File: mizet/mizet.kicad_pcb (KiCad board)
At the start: 2 copper layers, 41 parts, among them J1 USB_C_Receptacle_USB2.0_16P, J2 Conn_01x04, J3 Conn_01x12, J4 Conn_01x12, SW1 RotaryEncoder_Switch_MP, SW2 SW_Push, SW3 SW_Push, SW4 SW_Push, SW5 SW_Push, U1 RP2040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

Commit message: basic pcb
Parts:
- removed the R5 at (57.8, 52.1)
- removed the U2 at (55.0, 34.7)
- added D1: D_Schottky, Diode_SMD:D_SOD-123, B.Cu at (134.2, 87.8)
- added U1: XC6206PxxxMR, Package_TO_SOT_SMD:SOT-23-3, B.Cu at (135.9, 84.3)
- C1, C17, C2, J1, TP3, TP4, Y1: moved to B.Cu
- C10: renamed from C7; moved to B.Cu
- C11: renamed from C8; moved to B.Cu
- C12: renamed from C9; moved to B.Cu
- C13: renamed from C10; moved to B.Cu
- C14: renamed from C11; moved to B.Cu
- C15: renamed from C12; moved to B.Cu
- C16: renamed from C13; moved to B.Cu
- C3: renamed from C14; moved to B.Cu
- C4: renamed from C15; moved to B.Cu
- C5: renamed from C16; moved to B.Cu
- C6: renamed from C3; moved to B.Cu
- C7: renamed from C4; moved to B.Cu
- C8: renamed from C5; moved to B.Cu
- C9: renamed from C6; moved to B.Cu
- J3, J4: footprint Connector_PinSocket_2.54mm:PinSocket_1x12_P2.54mm_Vertical -> Connector_PinHeader_2.54mm:PinHeader_1x12_P2.54mm_Vertical; moved to B.Cu
- R1: renamed from R3; moved to B.Cu
- R2: renamed from R4; moved to B.Cu
- R3: renamed from R1; moved to B.Cu
- R4: renamed from R2; moved to B.Cu
- R5: renamed from R6; moved to B.Cu
- R6: renamed from R7; moved to B.Cu
- SW2, SW3, SW4, SW5: footprint Button_Switch_THT:SW_PUSH_1P1T_6x3.5mm_H4.3_APEM_MJTP1243 -> My_lib:tact_sw_smd
- TP1: renamed from TP2; moved to B.Cu
- TP2: renamed from TP1; moved to B.Cu
- U2: renamed from U1; footprint Package_DFN_QFN:QFN-56-1EP_7x7mm_P0.4mm_EP3.2x3.2mm -> My_lib:RP2040-QFN-56; moved to B.Cu
- U3: value AMS1117-3.3 -> W25Q16JVSS; footprint Package_TO_SOT_SMD:SOT-223-3_TabPin2 -> Package_SON:Winbond_USON-8-1EP_3x2mm_P0.5mm_EP0.2x1.6mm; moved to B.Cu
- moved SW1 150.7 mm to (179.2, 72.5), turned to -90 degrees
- moved TP3 139.7 mm to (182.3, 83.8)
- moved J2 135.3 mm to (166.3, 76.2)
- moved J4 134.8 mm to (138.3, 87.6), turned to -90 degrees
- moved TP4 133.1 mm to (176.7, 83.8)
- moved J3 131.8 mm to (138.3, 72.4), turned to -90 degrees
- moved TP1 131.3 mm to (171.1, 83.8)
- moved U2 125.1 mm to (151.1, 80.0), turned to -90 degrees
- moved C7 124.7 mm to (157.2, 81.4)
- moved C5 124.2 mm to (163.6, 80.4), turned to -90 degrees
- moved C4 121.7 mm to (160.9, 78.2), turned to 180 degrees
- moved C13 121.3 mm to (157.2, 80.5)
- moved C12 120.2 mm to (152.9, 85.2)
- moved U3 118.1 mm to (142.5, 76.2)
- moved SW2 116.2 mm to (128.0, 75.8)
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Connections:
- J3 pad 1: VBUS -> GP0
- J3 pad 10: GP14 -> GP9
- J3 pad 11: GP13 -> GP10
- J3 pad 12: GP12 -> GP11
- J3 pad 2: GND -> GP1
- J3 pad 3: +3V3 -> GP2
- J3 pad 4: GP29 -> GP3
- J3 pad 5: GP28 -> GP4
- J3 pad 6: GP27 -> GP5
- J3 pad 7: GP26 -> GP6
- J3 pad 8: GP25 -> GP7
- J3 pad 9: GP15 -> GP8
- J4 pad 1: GP0 -> VBUS
- J4 pad 10: GP9 -> GP20
- J4 pad 11: GP10 -> GP19
- J4 pad 12: GP11 -> GP18
- J4 pad 2: GP1 -> GND
- J4 pad 3: GP2 -> +3V3
- J4 pad 4: GP3 -> GP26
- J4 pad 5: GP4 -> GP25
- J4 pad 6: GP5 -> GP24
- J4 pad 7: GP6 -> GP23
- J4 pad 8: GP7 -> GP22
- J4 pad 9: GP8 -> GP21
- SW1 pad S1: RE_SW -> GND
- SW1 pad S2: GND -> RE_SW
- SW2 pad 1: SW_A -> GND
- SW2 pad 2: GND -> SW_A
- SW3 pad 1: SW_B -> GND
- SW3 pad 2: GND -> SW_B
- SW4 pad 1: SW_C -> GND
- SW4 pad 2: GND -> SW_C
- SW5 pad 1: SW_D -> GND
- SW5 pad 2: GND -> SW_D
- U2 pad 15: GP12 -> SDA
- U2 pad 16: GP13 -> SCL
- U2 pad 17: GP14 -> RE_B
- U2 pad 18: GP15 -> RE_A
- U2 pad 27: SDA -> RE_SW
- U2 pad 28: SCL -> SW_D
- U2 pad 29: RE_A -> GP18
- U2 pad 30: RE_B -> GP19
- U2 pad 31: RE_SW -> GP20
- U2 pad 32: SW_A -> GP21
- U2 pad 34: SW_B -> GP22
- U2 pad 35: SW_C -> GP23
- U2 pad 36: SW_D -> GP24
- U2 pad 39: GP27 -> SW_C
- U2 pad 40: GP28 -> SW_B
- U2 pad 41: GP29 -> SW_A
- U3 pad 1: GND -> QSPI_SS
- U3 pad 2: +3V3 -> QSPI_SD1
- U3 pad 3: VBUS -> QSPI_SD2
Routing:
- net +3V3: track 0.00 -> 91.1 mm, vias 0 -> 2
- net GND: track 0.00 -> 35.6 mm, vias 0 -> 12
- net Net-(U2-SWCLK): track 0.00 -> 30.8 mm, vias 0 -> 2
- net RE_A: track 0.00 -> 27.3 mm
- net SW_D: track 0.00 -> 25.7 mm, vias 0 -> 1
- net Net-(U2-SWD): track 0.00 -> 25.3 mm, vias 0 -> 2
- net SW_A: track 0.00 -> 24.9 mm, vias 0 -> 1
- net SW_B: track 0.00 -> 23.2 mm, vias 0 -> 1
- net SW_C: track 0.00 -> 22.4 mm, vias 0 -> 1
- net RE_B: track 0.00 -> 22.1 mm
- net RE_SW: track 0.00 -> 21.8 mm, vias 0 -> 1
- net +1V1: track 0.00 -> 18.9 mm, vias 0 -> 4
- net VBUS: track 0.00 -> 18.8 mm
- net Net-(U2-RUN): track 0.00 -> 18.7 mm, vias 0 -> 2
- net USB_D+: track 0.00 -> 17.1 mm
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- added copper zone on B.Cu, net +1V1
- added copper zone on B.Cu, net +3V3
- added copper zone on B.Cu, net GND
- added copper zone on F.Cu, net GND
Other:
- board outline added: 62.6 x 18.8 mm

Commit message: update pcb
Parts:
- added G***: LOGO, LOGO, B.Cu at (130.8, 73.8)
- TP3, TP4: footprint TestPoint:TestPoint_Pad_D1.5mm -> Connector_PinHeader_2.54mm:PinHeader_1x01_P2.54mm_Horizontal
- moved TP3 15.5 mm to (168.8, 76.2)
- moved TP4 7.91 mm to (168.8, 83.8)
- moved TP1 6.80 mm to (176.7, 80.0)
- moved TP2 1.57 mm to (135.1, 75.0), turned to 180 degrees
- moved SW5 1.05 mm to (133.5, 72.3)
- moved R1 0.15 mm to (133.1, 82.8)
- moved R2 0.15 mm to (133.1, 79.8)
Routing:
- net GND: track 35.6 -> 44.1 mm, vias 12 -> 20
- net Net-(U2-SWCLK): track 30.8 -> 23.5 mm, vias 2 -> 1
- net Net-(U2-SWD): track 25.3 -> 18.0 mm, vias 2 -> 1
- net Net-(U2-RUN): track 18.7 -> 25.8 mm
- net SW_D: track 25.7 -> 24.7 mm
- net Net-(R5-Pad2): track 2.38 -> 3.27 mm
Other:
- outline, holes or cut-outs redrawn
- board text added: "0"
- board text added: "1"
- board text added: "10"
- board text added: "11"
- board text added: "18"
- board text added: "19"
- board text added: "2"
- board text added: "20"
- board text added: "21"
- board text added: "22"
- board text added: "23"
- board text added: "24"
- board text added: "25"
- board text added: "26"
- board text added: "3"
- board text added: "3V3"
- board text added: "4"
- board text added: "5"
- board text added: "6"
- board text added: "7"
- board text added: "8"
- board text added: "9"
- board text added: "BOOT"
- board text added: "GND"
- board text added: "SWCLK"
- board text added: "SWDIO"
- board text added: "V_{BUS}"
- board text added: "mizet designed by object1037"
- board text added: "~{RESET}"

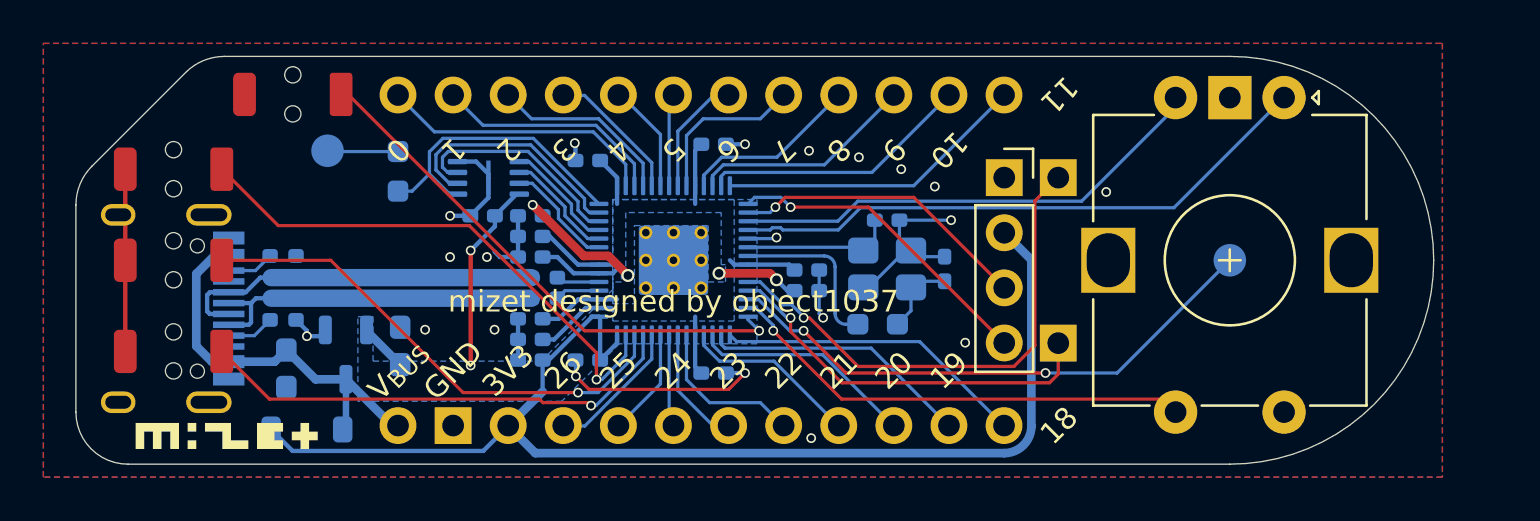
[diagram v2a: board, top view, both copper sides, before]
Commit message: add mounting holes
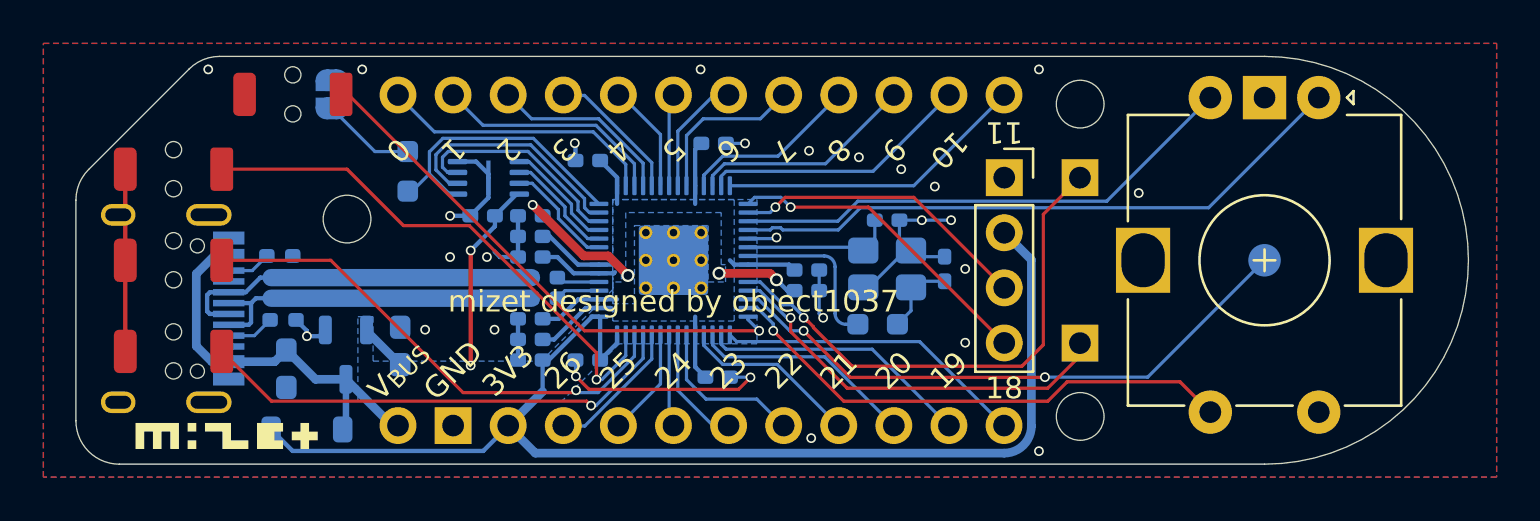
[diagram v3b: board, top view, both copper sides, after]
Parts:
- removed the TP2 at (135.1, 75.0)
- added H1: MountingHole, MountingHole:MountingHole_2.2mm_M2, F.Cu at (169.8, 87.2)
- added H2: MountingHole, MountingHole:MountingHole_2.2mm_M2, F.Cu at (136.0, 78.1)
- added H3: MountingHole, MountingHole:MountingHole_2.2mm_M2, F.Cu at (169.8, 72.8)
- added JP1: SolderJumper_2_Open, Jumper:SolderJumper-2_P1.3mm_Open_RoundedPad1.0x1.5mm, B.Cu at (135.3, 72.3)
- moved SW1 1.60 mm to (180.8, 72.5)
- moved TP1 1.60 mm to (178.3, 80.0)
- moved TP2 1.00 mm to (169.8, 76.2)
- moved TP3 1.00 mm to (169.8, 83.8)
- moved R5 0.45 mm to (138.8, 75.9)
- moved C12 0.27 mm to (153.1, 85.4)
- moved R2 0.15 mm to (132.9, 79.8)
- renumbered TP3 to TP2, TP4 to TP3
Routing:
- net RE_SW: track 21.8 -> 24.2 mm
- net Net-(U2-RUN): track 25.8 -> 27.5 mm
- net RE_A: track 27.3 -> 28.9 mm
- net RE_B: track 22.3 -> 23.7 mm
- net Net-(JP1-B): track 3.27 -> 4.32 mm
- net Net-(U2-SWD): track 18.0 -> 18.7 mm
- net Net-(U2-SWCLK): track 23.5 -> 24.1 mm
- net GND: track 44.1 -> 44.3 mm, vias 20 -> 27
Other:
- board size 62.6 x 18.8 mm -> 64.2 x 18.8 mm

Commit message: generate jlcpcb files
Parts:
- C1: value 10u -> 1u
- C2: value 22u -> 1u
- C4, C5: footprint Capacitor_SMD:C_0402_1005Metric_Pad0.74x0.62mm_HandSolder -> Capacitor_SMD:C_0603_1608Metric
- moved C4 0.25 mm to (160.9, 77.9)
- moved C5 0.20 mm to (163.8, 80.4)
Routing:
- net GND: track 44.3 -> 42.2 mm, vias 27 -> 26

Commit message: update
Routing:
- net GND: vias 26 -> 27
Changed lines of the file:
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@@
+	)
+	(via
+		(at 162.65 78.4)
+		(size 0.45)
+		(drill 0.3)
+		(layers "F.Cu" "B.Cu")
+		(free yes)
+		(net 1)
 	)
 	(via
